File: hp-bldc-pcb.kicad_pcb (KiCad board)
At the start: 4 copper layers, 93 x 53 mm, 109 parts, among them IC101 MCP1790-5002E/DB, IC401 PIC16F1936, IC601 BTN8962TA, IC631 BTN8962TA, IC661 BTN8962TA, T102 SBC817-40LT1G, T103 SBC817-40LT1G

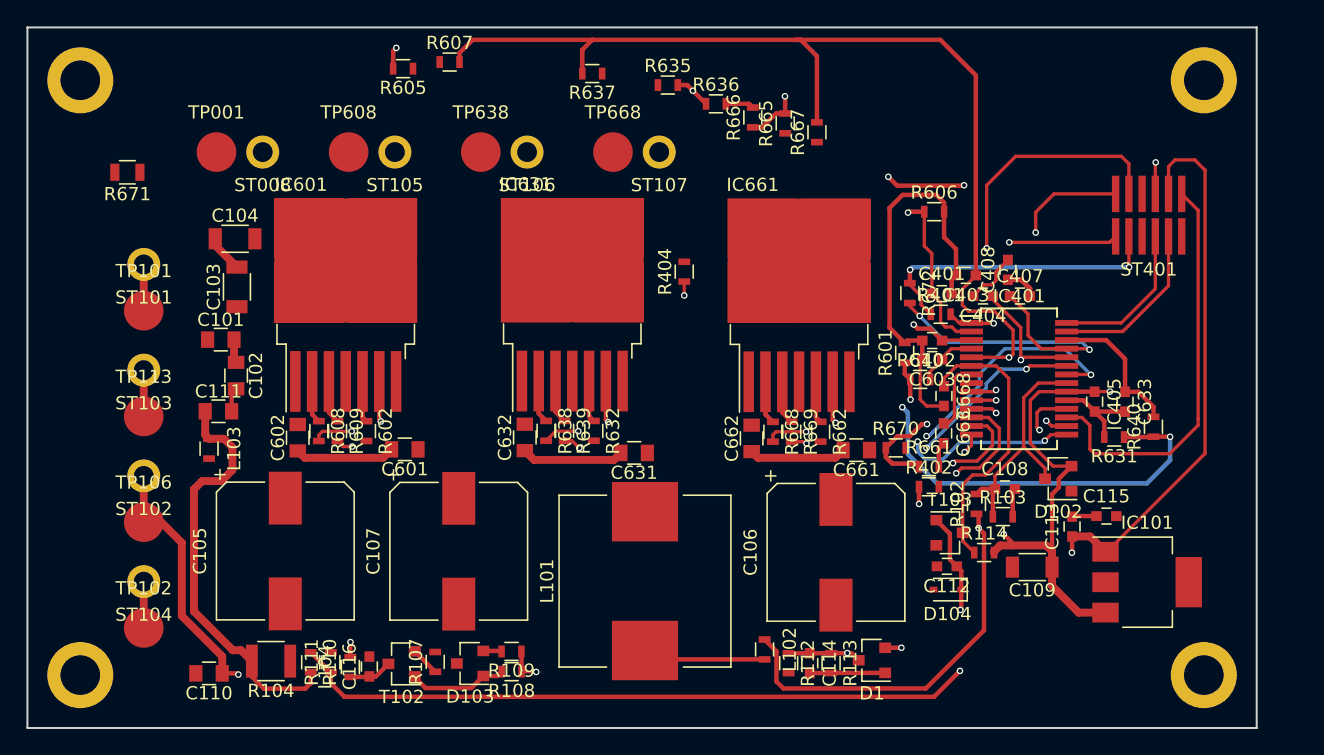
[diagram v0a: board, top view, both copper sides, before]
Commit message: - Finished putting down copper areas.
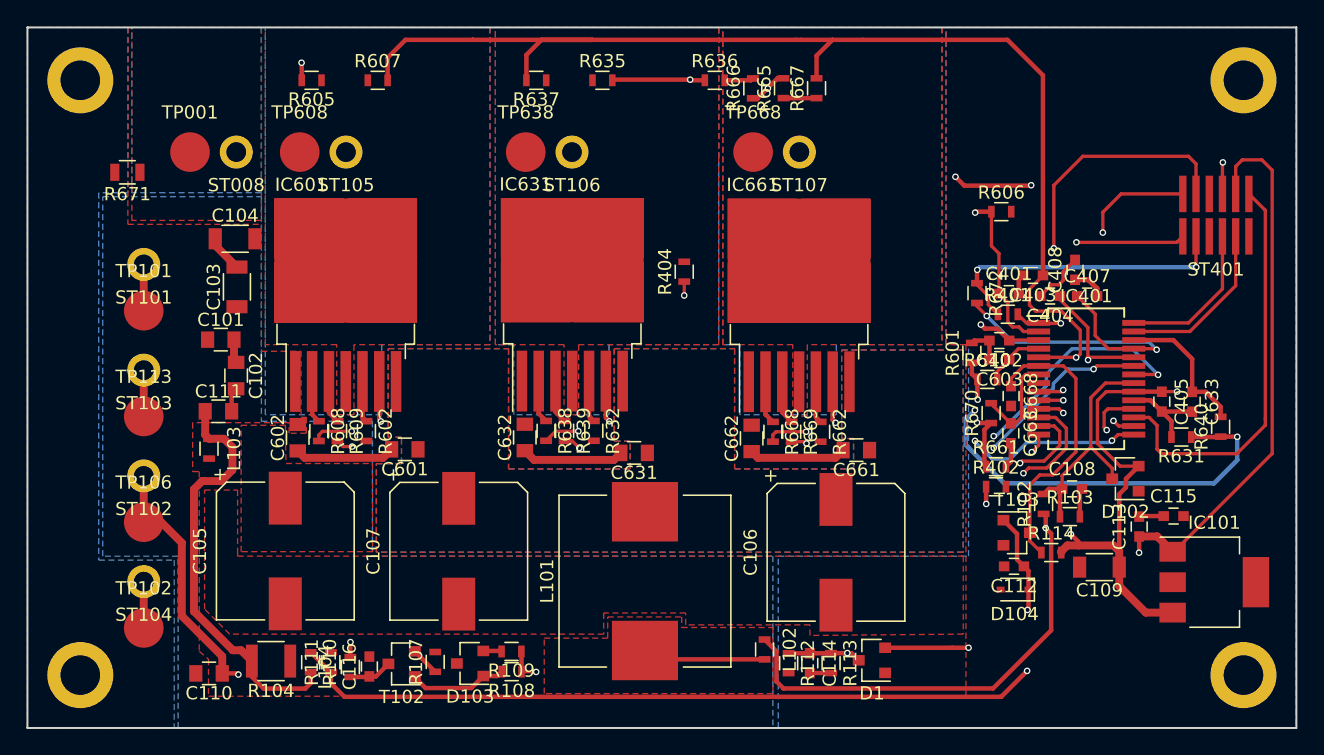
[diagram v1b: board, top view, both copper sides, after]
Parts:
- moved ST107 10.6 mm to (154.4, 78.4)
- moved TP668 10.6 mm to (150.9, 78.4)
- moved R670 7.68 mm to (168.9, 98.2), turned to 90 degrees
- moved R605 6.98 mm to (117.5, 73.0)
- moved R607 5.61 mm to (122.5, 73.0)
- moved C108 5.08 mm to (175.0, 103.9)
- moved C113 5.08 mm to (180.1, 106.8)
- moved C115 5.08 mm to (182.7, 106.0)
- moved C401 5.08 mm to (170.2, 89.1)
- moved C402 5.08 mm to (169.5, 92.7)
- moved C403 5.08 mm to (172.1, 87.8)
- moved C404 5.08 mm to (173.4, 89.3)
- moved C603 5.08 mm to (169.5, 94.1)
- moved C633 5.08 mm to (184.1, 97.3)
- moved C663 5.08 mm to (170.4, 99.7)
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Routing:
- net Earth: track 60.6 -> 30.4 mm
- net PH_1_V_SENSE: track 64.6 -> 77.2 mm
- net PH_SUM_SENSE: track 96.3 -> 108.8 mm
- net PH_2_V_SENSE: track 44.3 -> 54.3 mm
- net Net-(IC631-Pad6): track 56.5 -> 62.0 mm
- net PH_1_EN_FET: track 55.8 -> 61.3 mm
- net PH_1_DIR_FET: track 56.4 -> 61.6 mm
- net DIAG_MON: track 34.6 -> 39.7 mm
- net DIAG_PIC: track 54.2 -> 59.3 mm
- net Net-(C407-Pad1): track 55.0 -> 60.1 mm
- net PH_2_EN_FET: track 32.6 -> 37.7 mm
- net VBATT_2: track 79.8 -> 84.9 mm
- net Net-(IC601-Pad6): track 46.9 -> 52.0 mm
- net PH_3_DIR_FET: track 30.7 -> 35.8 mm
- net PH_2_DIR_FET: track 43.3 -> 48.4 mm
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- added copper zone on B.Cu, net Earth
- added copper zone on F.Cu, net Earth
- added copper zone on In1.Cu, net Earth
- added copper zone on In2.Cu, net Earth
- added copper zone on B.Cu, net Net-(R671-Pad1)
- added copper zone on F.Cu, net Net-(R671-Pad1)
- added copper zone on B.Cu, net PH_1
- added copper zone on F.Cu, net PH_1
- added copper zone on In1.Cu, net PH_1
- added copper zone on In2.Cu, net PH_1
- added copper zone on B.Cu, net PH_2
- added copper zone on F.Cu, net PH_2
- added copper zone on In1.Cu, net PH_2
- added copper zone on In2.Cu, net PH_2
- added copper zone on B.Cu, net PH_3
- added copper zone on F.Cu, net PH_3
- added copper zone on In1.Cu, net PH_3
- added copper zone on In2.Cu, net PH_3
- added copper zone on B.Cu, net VBATT
- added copper zone on F.Cu, net VBATT
- added copper zone on In2.Cu, net VBATT
- added copper zone on B.Cu, net VBATT_INT
- added copper zone on F.Cu, net VBATT_INT
- added copper zone on In2.Cu, net VBATT_INT
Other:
- board size 93 x 53 mm -> 96 x 53 mm

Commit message: - Almost done with PCB.  Need to fix a few errors.
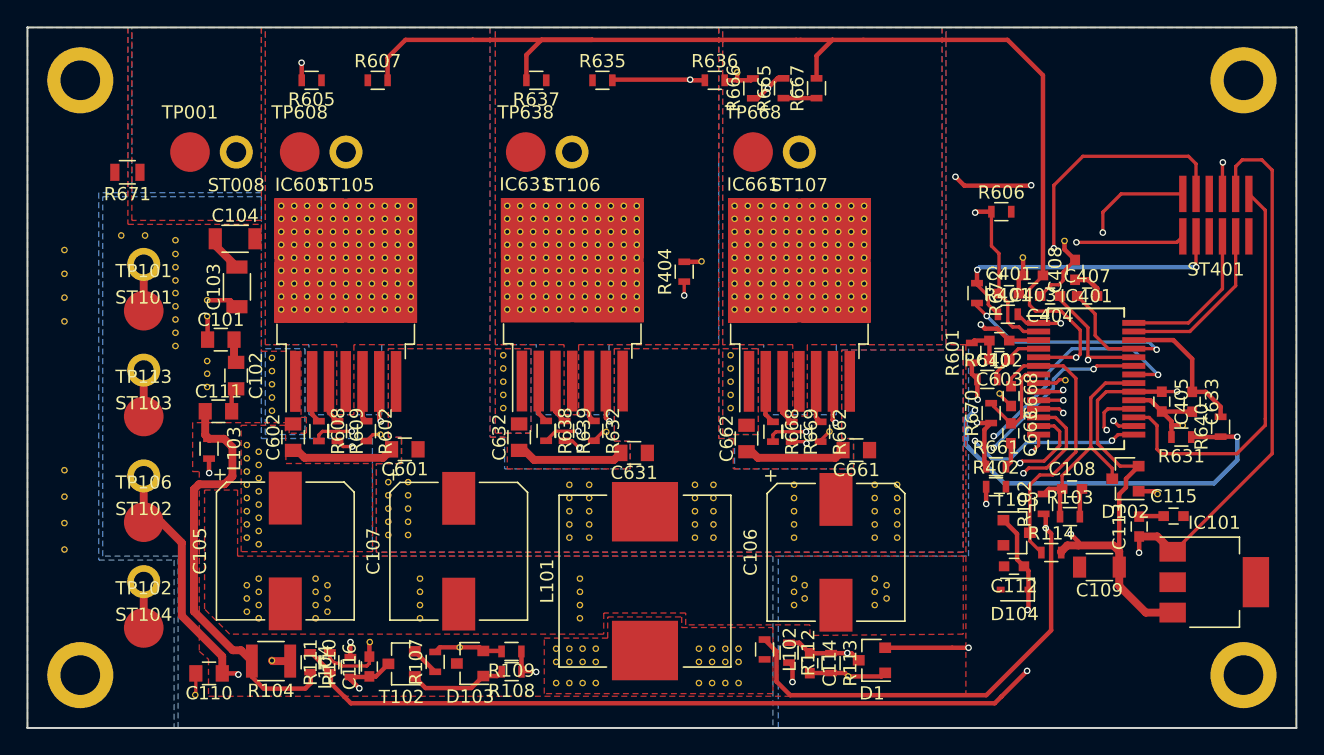
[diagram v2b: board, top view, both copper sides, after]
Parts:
- added REF**: VIA_0.3mm, hp-bldc-pcb:VIA_0.3mm, F.Cu at (174.5, 85.2)
- added REF**: VIA_0.3mm, hp-bldc-pcb:VIA_0.3mm, F.Cu at (161.0, 111.2)
- added REF**: VIA_0.3mm, hp-bldc-pcb:VIA_0.3mm, F.Cu at (147.9, 106.6)
- added REF**: VIA_0.3mm, hp-bldc-pcb:VIA_0.3mm, F.Cu at (147.9, 105.6)
- added REF**: VIA_0.3mm, hp-bldc-pcb:VIA_0.3mm, F.Cu at (147.9, 104.6)
- added REF**: VIA_0.3mm, hp-bldc-pcb:VIA_0.3mm, F.Cu at (147.9, 103.6)
- added REF**: VIA_0.3mm, hp-bldc-pcb:VIA_0.3mm, F.Cu at (146.5, 107.6)
- added REF**: VIA_0.3mm, hp-bldc-pcb:VIA_0.3mm, F.Cu at (146.5, 106.6)
- added REF**: VIA_0.3mm, hp-bldc-pcb:VIA_0.3mm, F.Cu at (146.5, 105.6)
- added REF**: VIA_0.3mm, hp-bldc-pcb:VIA_0.3mm, F.Cu at (146.5, 104.6)
- added REF**: VIA_0.3mm, hp-bldc-pcb:VIA_0.3mm, F.Cu at (146.5, 103.6)
- added REF**: VIA_0.3mm, hp-bldc-pcb:VIA_0.3mm, F.Cu at (138.5, 107.6)
- added REF**: VIA_0.3mm, hp-bldc-pcb:VIA_0.3mm, F.Cu at (160.1, 112.7)
- added REF**: VIA_0.3mm, hp-bldc-pcb:VIA_0.3mm, F.Cu at (138.5, 106.6)
- added REF**: VIA_0.3mm, hp-bldc-pcb:VIA_0.3mm, F.Cu at (138.5, 105.6)
- added REF**: VIA_0.3mm, hp-bldc-pcb:VIA_0.3mm, F.Cu at (138.5, 104.6)
- added REF**: VIA_0.3mm, hp-bldc-pcb:VIA_0.3mm, F.Cu at (138.5, 103.6)
- added REF**: VIA_0.3mm, hp-bldc-pcb:VIA_0.3mm, F.Cu at (137.0, 107.6)
- added REF**: VIA_0.3mm, hp-bldc-pcb:VIA_0.3mm, F.Cu at (137.0, 106.6)
- added REF**: VIA_0.3mm, hp-bldc-pcb:VIA_0.3mm, F.Cu at (137.0, 105.6)
- added REF**: VIA_0.3mm, hp-bldc-pcb:VIA_0.3mm, F.Cu at (137.0, 104.6)
- added REF**: VIA_0.3mm, hp-bldc-pcb:VIA_0.3mm, F.Cu at (137.0, 103.6)
- added REF**: VIA_0.3mm, hp-bldc-pcb:VIA_0.3mm, F.Cu at (124.8, 107.4)
- added REF**: VIA_0.3mm, hp-bldc-pcb:VIA_0.3mm, F.Cu at (160.1, 111.7)
- added REF**: VIA_0.3mm, hp-bldc-pcb:VIA_0.3mm, F.Cu at (124.8, 106.4)
- added REF**: VIA_0.3mm, hp-bldc-pcb:VIA_0.3mm, F.Cu at (124.8, 105.4)
- added REF**: VIA_0.3mm, hp-bldc-pcb:VIA_0.3mm, F.Cu at (124.8, 104.4)
- added REF**: VIA_0.3mm, hp-bldc-pcb:VIA_0.3mm, F.Cu at (124.8, 103.4)
- added REF**: VIA_0.3mm, hp-bldc-pcb:VIA_0.3mm, F.Cu at (123.3, 107.4)
- added REF**: VIA_0.3mm, hp-bldc-pcb:VIA_0.3mm, F.Cu at (123.3, 106.4)
- added REF**: VIA_0.3mm, hp-bldc-pcb:VIA_0.3mm, F.Cu at (123.3, 105.4)
- added REF**: VIA_0.3mm, hp-bldc-pcb:VIA_0.3mm, F.Cu at (123.3, 104.4)
- added REF**: VIA_0.3mm, hp-bldc-pcb:VIA_0.3mm, F.Cu at (123.3, 103.4)
- added REF**: VIA_0.3mm, hp-bldc-pcb:VIA_0.3mm, F.Cu at (112.6, 107.6)
- added REF**: VIA_0.3mm, hp-bldc-pcb:VIA_0.3mm, F.Cu at (160.1, 110.7)
- added REF**: VIA_0.3mm, hp-bldc-pcb:VIA_0.3mm, F.Cu at (112.6, 106.6)
- added REF**: VIA_0.3mm, hp-bldc-pcb:VIA_0.3mm, F.Cu at (112.6, 105.6)
- added REF**: VIA_0.3mm, hp-bldc-pcb:VIA_0.3mm, F.Cu at (112.6, 104.6)
- added REF**: VIA_0.3mm, hp-bldc-pcb:VIA_0.3mm, F.Cu at (112.6, 103.6)
- added REF**: VIA_0.3mm, hp-bldc-pcb:VIA_0.3mm, F.Cu at (112.6, 102.6)
- added REF**: VIA_0.3mm, hp-bldc-pcb:VIA_0.3mm, F.Cu at (112.6, 101.6)
- added REF**: VIA_0.3mm, hp-bldc-pcb:VIA_0.3mm, F.Cu at (112.6, 100.6)
- added REF**: VIA_0.3mm, hp-bldc-pcb:VIA_0.3mm, F.Cu at (113.5, 108.1)
- added REF**: VIA_0.3mm, hp-bldc-pcb:VIA_0.3mm, F.Cu at (113.5, 107.1)
- added REF**: VIA_0.3mm, hp-bldc-pcb:VIA_0.3mm, F.Cu at (113.5, 106.1)
- added REF**: VIA_0.3mm, hp-bldc-pcb:VIA_0.3mm, F.Cu at (154.8, 112.2)
- added REF**: VIA_0.3mm, hp-bldc-pcb:VIA_0.3mm, F.Cu at (113.5, 105.1)
- added REF**: VIA_0.3mm, hp-bldc-pcb:VIA_0.3mm, F.Cu at (113.5, 104.1)
- added REF**: VIA_0.3mm, hp-bldc-pcb:VIA_0.3mm, F.Cu at (113.5, 103.1)
- added REF**: VIA_0.3mm, hp-bldc-pcb:VIA_0.3mm, F.Cu at (113.5, 102.1)
- added REF**: VIA_0.3mm, hp-bldc-pcb:VIA_0.3mm, F.Cu at (113.5, 101.1)
- added REF**: VIA_0.3mm, hp-bldc-pcb:VIA_0.3mm, F.Cu at (107.2, 92.1)
- added REF**: VIA_0.3mm, hp-bldc-pcb:VIA_0.3mm, F.Cu at (107.2, 91.1)
- added REF**: VIA_0.3mm, hp-bldc-pcb:VIA_0.3mm, F.Cu at (107.2, 90.1)
- added REF**: VIA_0.3mm, hp-bldc-pcb:VIA_0.3mm, F.Cu at (107.2, 89.1)
- added REF**: VIA_0.3mm, hp-bldc-pcb:VIA_0.3mm, F.Cu at (107.2, 85.1)
- added REF**: VIA_0.3mm, hp-bldc-pcb:VIA_0.3mm, F.Cu at (154.8, 111.2)
- added REF**: VIA_0.3mm, hp-bldc-pcb:VIA_0.3mm, F.Cu at (103.1, 84.7)
- added REF**: VIA_0.3mm, hp-bldc-pcb:VIA_0.3mm, F.Cu at (109.6, 96.2)
- added REF**: VIA_0.3mm, hp-bldc-pcb:VIA_0.3mm, F.Cu at (109.6, 95.2)
- added REF**: VIA_0.3mm, hp-bldc-pcb:VIA_0.3mm, F.Cu at (109.6, 94.2)
- added REF**: VIA_0.3mm, hp-bldc-pcb:VIA_0.3mm, F.Cu at (109.6, 90.8)
- added REF**: VIA_0.3mm, hp-bldc-pcb:VIA_0.3mm, F.Cu at (109.6, 89.6)
- added REF**: VIA_0.3mm, hp-bldc-pcb:VIA_0.3mm, F.Cu at (114.5, 98.0)
- added REF**: VIA_0.3mm, hp-bldc-pcb:VIA_0.3mm, F.Cu at (114.5, 97.0)
- added REF**: VIA_0.3mm, hp-bldc-pcb:VIA_0.3mm, F.Cu at (114.5, 96.0)
- added REF**: VIA_0.3mm, hp-bldc-pcb:VIA_0.3mm, F.Cu at (114.5, 95.0)
- added REF**: VIA_0.3mm, hp-bldc-pcb:VIA_0.3mm, F.Cu at (154.0, 112.7)
- added REF**: VIA_0.3mm, hp-bldc-pcb:VIA_0.3mm, F.Cu at (114.5, 94.0)
- added REF**: VIA_0.3mm, hp-bldc-pcb:VIA_0.3mm, F.Cu at (132.0, 97.8)
- added REF**: VIA_0.3mm, hp-bldc-pcb:VIA_0.3mm, F.Cu at (132.0, 96.8)
- added REF**: VIA_0.3mm, hp-bldc-pcb:VIA_0.3mm, F.Cu at (132.0, 95.8)
- added REF**: VIA_0.3mm, hp-bldc-pcb:VIA_0.3mm, F.Cu at (132.0, 94.8)
- added REF**: VIA_0.3mm, hp-bldc-pcb:VIA_0.3mm, F.Cu at (132.0, 93.8)
- added REF**: VIA_0.3mm, hp-bldc-pcb:VIA_0.3mm, F.Cu at (149.2, 97.8)
- added REF**: VIA_0.3mm, hp-bldc-pcb:VIA_0.3mm, F.Cu at (149.2, 96.8)
- added REF**: VIA_0.3mm, hp-bldc-pcb:VIA_0.3mm, F.Cu at (149.2, 95.8)
- added REF**: VIA_0.3mm, hp-bldc-pcb:VIA_0.3mm, F.Cu at (149.2, 94.8)
- added REF**: VIA_0.3mm, hp-bldc-pcb:VIA_0.3mm, F.Cu at (154.0, 111.7)
- added REF**: VIA_0.3mm, hp-bldc-pcb:VIA_0.3mm, F.Cu at (149.2, 93.8)
- added REF**: VIA_0.3mm, hp-bldc-pcb:VIA_0.3mm, F.Cu at (147.0, 86.7)
- added REF**: VIA_0.3mm, hp-bldc-pcb:VIA_0.3mm, F.Cu at (149.7, 72.4)
- added REF**: VIA_0.3mm, hp-bldc-pcb:VIA_0.3mm, F.Cu at (125.0, 90.3)
- added REF**: VIA_0.3mm, hp-bldc-pcb:VIA_0.3mm, F.Cu at (125.0, 89.4)
- added REF**: VIA_0.3mm, hp-bldc-pcb:VIA_0.3mm, F.Cu at (125.0, 88.4)
- added REF**: VIA_0.3mm, hp-bldc-pcb:VIA_0.3mm, F.Cu at (125.0, 87.4)
- added REF**: VIA_0.3mm, hp-bldc-pcb:VIA_0.3mm, F.Cu at (125.0, 86.4)
- added REF**: VIA_0.3mm, hp-bldc-pcb:VIA_0.3mm, F.Cu at (125.0, 85.4)
- added REF**: VIA_0.3mm, hp-bldc-pcb:VIA_0.3mm, F.Cu at (125.0, 84.5)
- added REF**: VIA_0.3mm, hp-bldc-pcb:VIA_0.3mm, F.Cu at (154.0, 110.7)
- added REF**: VIA_0.3mm, hp-bldc-pcb:VIA_0.3mm, F.Cu at (125.0, 83.5)
- added REF**: VIA_0.3mm, hp-bldc-pcb:VIA_0.3mm, F.Cu at (125.0, 82.5)
- added REF**: VIA_0.3mm, hp-bldc-pcb:VIA_0.3mm, F.Cu at (124.0, 90.3)
- added REF**: VIA_0.3mm, hp-bldc-pcb:VIA_0.3mm, F.Cu at (124.0, 89.4)
- added REF**: VIA_0.3mm, hp-bldc-pcb:VIA_0.3mm, F.Cu at (124.0, 88.4)
- added REF**: VIA_0.3mm, hp-bldc-pcb:VIA_0.3mm, F.Cu at (124.0, 87.4)
- added REF**: VIA_0.3mm, hp-bldc-pcb:VIA_0.3mm, F.Cu at (124.0, 86.4)
- added REF**: VIA_0.3mm, hp-bldc-pcb:VIA_0.3mm, F.Cu at (124.0, 85.4)
- added REF**: VIA_0.3mm, hp-bldc-pcb:VIA_0.3mm, F.Cu at (124.0, 84.5)
- added REF**: VIA_0.3mm, hp-bldc-pcb:VIA_0.3mm, F.Cu at (124.0, 83.5)
- added REF**: VIA_0.3mm, hp-bldc-pcb:VIA_0.3mm, F.Cu at (137.8, 113.7)
- added REF**: VIA_0.3mm, hp-bldc-pcb:VIA_0.3mm, F.Cu at (124.0, 82.5)
- added REF**: VIA_0.3mm, hp-bldc-pcb:VIA_0.3mm, F.Cu at (123.0, 90.3)
- added REF**: VIA_0.3mm, hp-bldc-pcb:VIA_0.3mm, F.Cu at (123.0, 89.4)
- added REF**: VIA_0.3mm, hp-bldc-pcb:VIA_0.3mm, F.Cu at (123.0, 88.4)
- added REF**: VIA_0.3mm, hp-bldc-pcb:VIA_0.3mm, F.Cu at (123.0, 87.4)
- added REF**: VIA_0.3mm, hp-bldc-pcb:VIA_0.3mm, F.Cu at (123.0, 86.4)
- added REF**: VIA_0.3mm, hp-bldc-pcb:VIA_0.3mm, F.Cu at (123.0, 85.4)
- added REF**: VIA_0.3mm, hp-bldc-pcb:VIA_0.3mm, F.Cu at (123.0, 84.5)
- added REF**: VIA_0.3mm, hp-bldc-pcb:VIA_0.3mm, F.Cu at (123.0, 83.5)
- added REF**: VIA_0.3mm, hp-bldc-pcb:VIA_0.3mm, F.Cu at (123.0, 82.5)
- added REF**: VIA_0.3mm, hp-bldc-pcb:VIA_0.3mm, F.Cu at (171.3, 86.4)
- added REF**: VIA_0.3mm, hp-bldc-pcb:VIA_0.3mm, F.Cu at (137.8, 112.7)
- added REF**: VIA_0.3mm, hp-bldc-pcb:VIA_0.3mm, F.Cu at (122.1, 90.3)
- added REF**: VIA_0.3mm, hp-bldc-pcb:VIA_0.3mm, F.Cu at (122.1, 89.4)
- added REF**: VIA_0.3mm, hp-bldc-pcb:VIA_0.3mm, F.Cu at (122.1, 88.4)
- added REF**: VIA_0.3mm, hp-bldc-pcb:VIA_0.3mm, F.Cu at (122.1, 87.4)
- added REF**: VIA_0.3mm, hp-bldc-pcb:VIA_0.3mm, F.Cu at (122.1, 86.4)
- added REF**: VIA_0.3mm, hp-bldc-pcb:VIA_0.3mm, F.Cu at (122.1, 85.4)
- added REF**: VIA_0.3mm, hp-bldc-pcb:VIA_0.3mm, F.Cu at (122.1, 84.5)
- added REF**: VIA_0.3mm, hp-bldc-pcb:VIA_0.3mm, F.Cu at (122.1, 83.5)
- added REF**: VIA_0.3mm, hp-bldc-pcb:VIA_0.3mm, F.Cu at (122.1, 82.5)
- added REF**: VIA_0.3mm, hp-bldc-pcb:VIA_0.3mm, F.Cu at (121.1, 90.3)
- added REF**: VIA_0.3mm, hp-bldc-pcb:VIA_0.3mm, F.Cu at (137.8, 111.7)
- added REF**: VIA_0.3mm, hp-bldc-pcb:VIA_0.3mm, F.Cu at (121.1, 89.4)
- added REF**: VIA_0.3mm, hp-bldc-pcb:VIA_0.3mm, F.Cu at (121.1, 88.4)
- added REF**: VIA_0.3mm, hp-bldc-pcb:VIA_0.3mm, F.Cu at (121.1, 87.4)
- added REF**: VIA_0.3mm, hp-bldc-pcb:VIA_0.3mm, F.Cu at (121.1, 86.4)
- added REF**: VIA_0.3mm, hp-bldc-pcb:VIA_0.3mm, F.Cu at (121.1, 85.4)
- added REF**: VIA_0.3mm, hp-bldc-pcb:VIA_0.3mm, F.Cu at (121.1, 84.5)
- added REF**: VIA_0.3mm, hp-bldc-pcb:VIA_0.3mm, F.Cu at (121.1, 83.5)
- added REF**: VIA_0.3mm, hp-bldc-pcb:VIA_0.3mm, F.Cu at (121.1, 82.5)
- added REF**: VIA_0.3mm, hp-bldc-pcb:VIA_0.3mm, F.Cu at (120.1, 90.3)
- added REF**: VIA_0.3mm, hp-bldc-pcb:VIA_0.3mm, F.Cu at (120.1, 89.4)
- added REF**: VIA_0.3mm, hp-bldc-pcb:VIA_0.3mm, F.Cu at (137.8, 110.7)
- added REF**: VIA_0.3mm, hp-bldc-pcb:VIA_0.3mm, F.Cu at (120.1, 88.4)
- added REF**: VIA_0.3mm, hp-bldc-pcb:VIA_0.3mm, F.Cu at (120.1, 87.4)
- added REF**: VIA_0.3mm, hp-bldc-pcb:VIA_0.3mm, F.Cu at (120.1, 86.4)
- added REF**: VIA_0.3mm, hp-bldc-pcb:VIA_0.3mm, F.Cu at (120.1, 85.4)
- added REF**: VIA_0.3mm, hp-bldc-pcb:VIA_0.3mm, F.Cu at (120.1, 84.5)
- added REF**: VIA_0.3mm, hp-bldc-pcb:VIA_0.3mm, F.Cu at (120.1, 83.5)
- added REF**: VIA_0.3mm, hp-bldc-pcb:VIA_0.3mm, F.Cu at (120.1, 82.5)
- added REF**: VIA_0.3mm, hp-bldc-pcb:VIA_0.3mm, F.Cu at (119.1, 90.3)
- added REF**: VIA_0.3mm, hp-bldc-pcb:VIA_0.3mm, F.Cu at (119.1, 89.4)
- added REF**: VIA_0.3mm, hp-bldc-pcb:VIA_0.3mm, F.Cu at (119.1, 88.4)
- added REF**: VIA_0.3mm, hp-bldc-pcb:VIA_0.3mm, F.Cu at (125.7, 113.7)
- added REF**: VIA_0.3mm, hp-bldc-pcb:VIA_0.3mm, F.Cu at (119.1, 87.4)
- added REF**: VIA_0.3mm, hp-bldc-pcb:VIA_0.3mm, F.Cu at (119.1, 86.4)
- added REF**: VIA_0.3mm, hp-bldc-pcb:VIA_0.3mm, F.Cu at (119.1, 85.4)
- added REF**: VIA_0.3mm, hp-bldc-pcb:VIA_0.3mm, F.Cu at (119.1, 84.5)
- added REF**: VIA_0.3mm, hp-bldc-pcb:VIA_0.3mm, F.Cu at (119.1, 83.5)
- added REF**: VIA_0.3mm, hp-bldc-pcb:VIA_0.3mm, F.Cu at (119.1, 82.5)
- added REF**: VIA_0.3mm, hp-bldc-pcb:VIA_0.3mm, F.Cu at (118.1, 90.3)
- added REF**: VIA_0.3mm, hp-bldc-pcb:VIA_0.3mm, F.Cu at (118.1, 89.4)
- added REF**: VIA_0.3mm, hp-bldc-pcb:VIA_0.3mm, F.Cu at (118.1, 88.4)
- added REF**: VIA_0.3mm, hp-bldc-pcb:VIA_0.3mm, F.Cu at (118.1, 87.4)
- added REF**: VIA_0.3mm, hp-bldc-pcb:VIA_0.3mm, F.Cu at (125.7, 112.7)
- added REF**: VIA_0.3mm, hp-bldc-pcb:VIA_0.3mm, F.Cu at (118.1, 86.4)
- added REF**: VIA_0.3mm, hp-bldc-pcb:VIA_0.3mm, F.Cu at (118.1, 85.4)
- added REF**: VIA_0.3mm, hp-bldc-pcb:VIA_0.3mm, F.Cu at (118.1, 84.5)
- added REF**: VIA_0.3mm, hp-bldc-pcb:VIA_0.3mm, F.Cu at (118.1, 83.5)
- added REF**: VIA_0.3mm, hp-bldc-pcb:VIA_0.3mm, F.Cu at (118.1, 82.5)
- added REF**: VIA_0.3mm, hp-bldc-pcb:VIA_0.3mm, F.Cu at (117.2, 90.3)
- added REF**: VIA_0.3mm, hp-bldc-pcb:VIA_0.3mm, F.Cu at (117.2, 89.4)
- added REF**: VIA_0.3mm, hp-bldc-pcb:VIA_0.3mm, F.Cu at (117.2, 88.4)
- added REF**: VIA_0.3mm, hp-bldc-pcb:VIA_0.3mm, F.Cu at (117.2, 87.4)
- added REF**: VIA_0.3mm, hp-bldc-pcb:VIA_0.3mm, F.Cu at (117.2, 86.4)
- added REF**: VIA_0.3mm, hp-bldc-pcb:VIA_0.3mm, F.Cu at (125.7, 111.7)
- added REF**: VIA_0.3mm, hp-bldc-pcb:VIA_0.3mm, F.Cu at (117.2, 85.4)
- added REF**: VIA_0.3mm, hp-bldc-pcb:VIA_0.3mm, F.Cu at (117.2, 84.5)
- added REF**: VIA_0.3mm, hp-bldc-pcb:VIA_0.3mm, F.Cu at (117.2, 83.5)
- added REF**: VIA_0.3mm, hp-bldc-pcb:VIA_0.3mm, F.Cu at (117.2, 82.5)
- added REF**: VIA_0.3mm, hp-bldc-pcb:VIA_0.3mm, F.Cu at (116.2, 90.3)
- added REF**: VIA_0.3mm, hp-bldc-pcb:VIA_0.3mm, F.Cu at (116.2, 89.4)
- added REF**: VIA_0.3mm, hp-bldc-pcb:VIA_0.3mm, F.Cu at (116.2, 88.4)
- added REF**: VIA_0.3mm, hp-bldc-pcb:VIA_0.3mm, F.Cu at (116.2, 87.4)
- added REF**: VIA_0.3mm, hp-bldc-pcb:VIA_0.3mm, F.Cu at (116.2, 86.4)
- added REF**: VIA_0.3mm, hp-bldc-pcb:VIA_0.3mm, F.Cu at (116.2, 85.4)
- added REF**: VIA_0.3mm, hp-bldc-pcb:VIA_0.3mm, F.Cu at (125.7, 110.7)
- added REF**: VIA_0.3mm, hp-bldc-pcb:VIA_0.3mm, F.Cu at (116.2, 84.5)
- added REF**: VIA_0.3mm, hp-bldc-pcb:VIA_0.3mm, F.Cu at (116.2, 83.5)
- added REF**: VIA_0.3mm, hp-bldc-pcb:VIA_0.3mm, F.Cu at (116.2, 82.5)
- added REF**: VIA_0.3mm, hp-bldc-pcb:VIA_0.3mm, F.Cu at (115.2, 90.3)
- added REF**: VIA_0.3mm, hp-bldc-pcb:VIA_0.3mm, F.Cu at (115.2, 89.4)
- added REF**: VIA_0.3mm, hp-bldc-pcb:VIA_0.3mm, F.Cu at (115.2, 88.4)
- added REF**: VIA_0.3mm, hp-bldc-pcb:VIA_0.3mm, F.Cu at (115.2, 87.4)
- added REF**: VIA_0.3mm, hp-bldc-pcb:VIA_0.3mm, F.Cu at (115.2, 86.4)
- added REF**: VIA_0.3mm, hp-bldc-pcb:VIA_0.3mm, F.Cu at (115.2, 85.4)
- added REF**: VIA_0.3mm, hp-bldc-pcb:VIA_0.3mm, F.Cu at (115.2, 84.5)
- added REF**: VIA_0.3mm, hp-bldc-pcb:VIA_0.3mm, F.Cu at (118.7, 113.2)
- added REF**: VIA_0.3mm, hp-bldc-pcb:VIA_0.3mm, F.Cu at (115.2, 83.5)
- added REF**: VIA_0.3mm, hp-bldc-pcb:VIA_0.3mm, F.Cu at (115.2, 82.5)
- added REF**: VIA_0.3mm, hp-bldc-pcb:VIA_0.3mm, F.Cu at (149.5, 82.5)
- added REF**: VIA_0.3mm, hp-bldc-pcb:VIA_0.3mm, F.Cu at (142.1, 90.3)
- added REF**: VIA_0.3mm, hp-bldc-pcb:VIA_0.3mm, F.Cu at (142.1, 89.4)
- added REF**: VIA_0.3mm, hp-bldc-pcb:VIA_0.3mm, F.Cu at (142.1, 88.4)
- added REF**: VIA_0.3mm, hp-bldc-pcb:VIA_0.3mm, F.Cu at (142.1, 87.4)
- added REF**: VIA_0.3mm, hp-bldc-pcb:VIA_0.3mm, F.Cu at (142.1, 86.4)
- added REF**: VIA_0.3mm, hp-bldc-pcb:VIA_0.3mm, F.Cu at (142.1, 85.4)
- added REF**: VIA_0.3mm, hp-bldc-pcb:VIA_0.3mm, F.Cu at (142.1, 84.5)
- added REF**: VIA_0.3mm, hp-bldc-pcb:VIA_0.3mm, F.Cu at (118.7, 112.2)
- added REF**: VIA_0.3mm, hp-bldc-pcb:VIA_0.3mm, F.Cu at (142.1, 83.5)
- added REF**: VIA_0.3mm, hp-bldc-pcb:VIA_0.3mm, F.Cu at (142.1, 82.5)
- added REF**: VIA_0.3mm, hp-bldc-pcb:VIA_0.3mm, F.Cu at (141.1, 90.3)
- added REF**: VIA_0.3mm, hp-bldc-pcb:VIA_0.3mm, F.Cu at (141.1, 89.4)
- added REF**: VIA_0.3mm, hp-bldc-pcb:VIA_0.3mm, F.Cu at (141.1, 88.4)
- added REF**: VIA_0.3mm, hp-bldc-pcb:VIA_0.3mm, F.Cu at (141.1, 87.4)
- added REF**: VIA_0.3mm, hp-bldc-pcb:VIA_0.3mm, F.Cu at (141.1, 86.4)
- added REF**: VIA_0.3mm, hp-bldc-pcb:VIA_0.3mm, F.Cu at (141.1, 85.4)
- added REF**: VIA_0.3mm, hp-bldc-pcb:VIA_0.3mm, F.Cu at (141.1, 84.5)
- added REF**: VIA_0.3mm, hp-bldc-pcb:VIA_0.3mm, F.Cu at (141.1, 83.5)
- added REF**: VIA_0.3mm, hp-bldc-pcb:VIA_0.3mm, F.Cu at (118.7, 111.2)
- added REF**: VIA_0.3mm, hp-bldc-pcb:VIA_0.3mm, F.Cu at (141.1, 82.5)
- added REF**: VIA_0.3mm, hp-bldc-pcb:VIA_0.3mm, F.Cu at (140.1, 90.3)
- added REF**: VIA_0.3mm, hp-bldc-pcb:VIA_0.3mm, F.Cu at (140.1, 89.4)
- added REF**: VIA_0.3mm, hp-bldc-pcb:VIA_0.3mm, F.Cu at (140.1, 88.4)
- added REF**: VIA_0.3mm, hp-bldc-pcb:VIA_0.3mm, F.Cu at (140.1, 87.4)
- added REF**: VIA_0.3mm, hp-bldc-pcb:VIA_0.3mm, F.Cu at (140.1, 86.4)
- added REF**: VIA_0.3mm, hp-bldc-pcb:VIA_0.3mm, F.Cu at (140.1, 85.4)
- added REF**: VIA_0.3mm, hp-bldc-pcb:VIA_0.3mm, F.Cu at (140.1, 84.5)
- added REF**: VIA_0.3mm, hp-bldc-pcb:VIA_0.3mm, F.Cu at (140.1, 83.5)
- added REF**: VIA_0.3mm, hp-bldc-pcb:VIA_0.3mm, F.Cu at (140.1, 82.5)
- added REF**: VIA_0.3mm, hp-bldc-pcb:VIA_0.3mm, F.Cu at (169.6, 96.7)
- added REF**: VIA_0.3mm, hp-bldc-pcb:VIA_0.3mm, F.Cu at (117.8, 113.7)
- added REF**: VIA_0.3mm, hp-bldc-pcb:VIA_0.3mm, F.Cu at (139.2, 90.3)
- added REF**: VIA_0.3mm, hp-bldc-pcb:VIA_0.3mm, F.Cu at (139.2, 89.4)
- added REF**: VIA_0.3mm, hp-bldc-pcb:VIA_0.3mm, F.Cu at (139.2, 88.4)
- added REF**: VIA_0.3mm, hp-bldc-pcb:VIA_0.3mm, F.Cu at (139.2, 87.4)
- added REF**: VIA_0.3mm, hp-bldc-pcb:VIA_0.3mm, F.Cu at (139.2, 86.4)
- added REF**: VIA_0.3mm, hp-bldc-pcb:VIA_0.3mm, F.Cu at (139.2, 85.4)
- added REF**: VIA_0.3mm, hp-bldc-pcb:VIA_0.3mm, F.Cu at (139.2, 84.5)
- added REF**: VIA_0.3mm, hp-bldc-pcb:VIA_0.3mm, F.Cu at (139.2, 83.5)
- added REF**: VIA_0.3mm, hp-bldc-pcb:VIA_0.3mm, F.Cu at (139.2, 82.5)
- added REF**: VIA_0.3mm, hp-bldc-pcb:VIA_0.3mm, F.Cu at (138.2, 90.3)
- added REF**: VIA_0.3mm, hp-bldc-pcb:VIA_0.3mm, F.Cu at (117.8, 112.7)
- added REF**: VIA_0.3mm, hp-bldc-pcb:VIA_0.3mm, F.Cu at (138.2, 89.4)
- added REF**: VIA_0.3mm, hp-bldc-pcb:VIA_0.3mm, F.Cu at (138.2, 88.4)
- added REF**: VIA_0.3mm, hp-bldc-pcb:VIA_0.3mm, F.Cu at (138.2, 87.4)
- added REF**: VIA_0.3mm, hp-bldc-pcb:VIA_0.3mm, F.Cu at (138.2, 86.4)
- added REF**: VIA_0.3mm, hp-bldc-pcb:VIA_0.3mm, F.Cu at (138.2, 85.4)
- added REF**: VIA_0.3mm, hp-bldc-pcb:VIA_0.3mm, F.Cu at (138.2, 84.5)
- added REF**: VIA_0.3mm, hp-bldc-pcb:VIA_0.3mm, F.Cu at (138.2, 83.5)
- added REF**: VIA_0.3mm, hp-bldc-pcb:VIA_0.3mm, F.Cu at (138.2, 82.5)
- added REF**: VIA_0.3mm, hp-bldc-pcb:VIA_0.3mm, F.Cu at (137.2, 90.3)
- added REF**: VIA_0.3mm, hp-bldc-pcb:VIA_0.3mm, F.Cu at (137.2, 89.4)
- added REF**: VIA_0.3mm, hp-bldc-pcb:VIA_0.3mm, F.Cu at (117.8, 111.7)
- added REF**: VIA_0.3mm, hp-bldc-pcb:VIA_0.3mm, F.Cu at (137.2, 88.4)
- added REF**: VIA_0.3mm, hp-bldc-pcb:VIA_0.3mm, F.Cu at (137.2, 87.4)
- added REF**: VIA_0.3mm, hp-bldc-pcb:VIA_0.3mm, F.Cu at (137.2, 86.4)
- added REF**: VIA_0.3mm, hp-bldc-pcb:VIA_0.3mm, F.Cu at (137.2, 85.4)
- added REF**: VIA_0.3mm, hp-bldc-pcb:VIA_0.3mm, F.Cu at (137.2, 84.5)
- added REF**: VIA_0.3mm, hp-bldc-pcb:VIA_0.3mm, F.Cu at (137.2, 83.5)
- added REF**: VIA_0.3mm, hp-bldc-pcb:VIA_0.3mm, F.Cu at (137.2, 82.5)
- added REF**: VIA_0.3mm, hp-bldc-pcb:VIA_0.3mm, F.Cu at (136.2, 90.3)
- added REF**: VIA_0.3mm, hp-bldc-pcb:VIA_0.3mm, F.Cu at (136.2, 89.4)
- added REF**: VIA_0.3mm, hp-bldc-pcb:VIA_0.3mm, F.Cu at (136.2, 88.4)
- added REF**: VIA_0.3mm, hp-bldc-pcb:VIA_0.3mm, F.Cu at (117.8, 110.7)
- added REF**: VIA_0.3mm, hp-bldc-pcb:VIA_0.3mm, F.Cu at (136.2, 87.4)
- added REF**: VIA_0.3mm, hp-bldc-pcb:VIA_0.3mm, F.Cu at (136.2, 86.4)
- added REF**: VIA_0.3mm, hp-bldc-pcb:VIA_0.3mm, F.Cu at (136.2, 85.4)
- added REF**: VIA_0.3mm, hp-bldc-pcb:VIA_0.3mm, F.Cu at (136.2, 84.5)
- added REF**: VIA_0.3mm, hp-bldc-pcb:VIA_0.3mm, F.Cu at (136.2, 83.5)
- added REF**: VIA_0.3mm, hp-bldc-pcb:VIA_0.3mm, F.Cu at (136.2, 82.5)
- added REF**: VIA_0.3mm, hp-bldc-pcb:VIA_0.3mm, F.Cu at (135.2, 90.3)
- added REF**: VIA_0.3mm, hp-bldc-pcb:VIA_0.3mm, F.Cu at (135.2, 89.4)
- added REF**: VIA_0.3mm, hp-bldc-pcb:VIA_0.3mm, F.Cu at (135.2, 88.4)
- added REF**: VIA_0.3mm, hp-bldc-pcb:VIA_0.3mm, F.Cu at (135.2, 87.4)
- added REF**: VIA_0.3mm, hp-bldc-pcb:VIA_0.3mm, F.Cu at (112.6, 113.2)
- added REF**: VIA_0.3mm, hp-bldc-pcb:VIA_0.3mm, F.Cu at (135.2, 86.4)
- added REF**: VIA_0.3mm, hp-bldc-pcb:VIA_0.3mm, F.Cu at (135.2, 85.4)
- added REF**: VIA_0.3mm, hp-bldc-pcb:VIA_0.3mm, F.Cu at (135.2, 84.5)
- added REF**: VIA_0.3mm, hp-bldc-pcb:VIA_0.3mm, F.Cu at (135.2, 83.5)
- added REF**: VIA_0.3mm, hp-bldc-pcb:VIA_0.3mm, F.Cu at (135.2, 82.5)
- added REF**: VIA_0.3mm, hp-bldc-pcb:VIA_0.3mm, F.Cu at (134.3, 90.3)
- added REF**: VIA_0.3mm, hp-bldc-pcb:VIA_0.3mm, F.Cu at (134.3, 89.4)
- added REF**: VIA_0.3mm, hp-bldc-pcb:VIA_0.3mm, F.Cu at (134.3, 88.4)
- added REF**: VIA_0.3mm, hp-bldc-pcb:VIA_0.3mm, F.Cu at (134.3, 87.4)
- added REF**: VIA_0.3mm, hp-bldc-pcb:VIA_0.3mm, F.Cu at (134.3, 86.4)
- added REF**: VIA_0.3mm, hp-bldc-pcb:VIA_0.3mm, F.Cu at (112.6, 112.2)
- added REF**: VIA_0.3mm, hp-bldc-pcb:VIA_0.3mm, F.Cu at (134.3, 85.4)
- added REF**: VIA_0.3mm, hp-bldc-pcb:VIA_0.3mm, F.Cu at (134.3, 84.5)
- added REF**: VIA_0.3mm, hp-bldc-pcb:VIA_0.3mm, F.Cu at (134.3, 83.5)
- added REF**: VIA_0.3mm, hp-bldc-pcb:VIA_0.3mm, F.Cu at (134.3, 82.5)
- added REF**: VIA_0.3mm, hp-bldc-pcb:VIA_0.3mm, F.Cu at (133.3, 90.3)
- added REF**: VIA_0.3mm, hp-bldc-pcb:VIA_0.3mm, F.Cu at (133.3, 89.4)
- added REF**: VIA_0.3mm, hp-bldc-pcb:VIA_0.3mm, F.Cu at (133.3, 88.4)
- added REF**: VIA_0.3mm, hp-bldc-pcb:VIA_0.3mm, F.Cu at (133.3, 87.4)
- added REF**: VIA_0.3mm, hp-bldc-pcb:VIA_0.3mm, F.Cu at (133.3, 86.4)
- added REF**: VIA_0.3mm, hp-bldc-pcb:VIA_0.3mm, F.Cu at (133.3, 85.4)
- added REF**: VIA_0.3mm, hp-bldc-pcb:VIA_0.3mm, F.Cu at (112.6, 111.2)
- added REF**: VIA_0.3mm, hp-bldc-pcb:VIA_0.3mm, F.Cu at (133.3, 84.5)
- added REF**: VIA_0.3mm, hp-bldc-pcb:VIA_0.3mm, F.Cu at (133.3, 83.5)
- added REF**: VIA_0.3mm, hp-bldc-pcb:VIA_0.3mm, F.Cu at (133.3, 82.5)
- added REF**: VIA_0.3mm, hp-bldc-pcb:VIA_0.3mm, F.Cu at (132.3, 90.3)
- added REF**: VIA_0.3mm, hp-bldc-pcb:VIA_0.3mm, F.Cu at (132.3, 89.4)
- added REF**: VIA_0.3mm, hp-bldc-pcb:VIA_0.3mm, F.Cu at (132.3, 88.4)
- added REF**: VIA_0.3mm, hp-bldc-pcb:VIA_0.3mm, F.Cu at (132.3, 87.4)
- added REF**: VIA_0.3mm, hp-bldc-pcb:VIA_0.3mm, F.Cu at (132.3, 86.4)
- added REF**: VIA_0.3mm, hp-bldc-pcb:VIA_0.3mm, F.Cu at (132.3, 85.4)
- added REF**: VIA_0.3mm, hp-bldc-pcb:VIA_0.3mm, F.Cu at (132.3, 84.5)
- added REF**: VIA_0.3mm, hp-bldc-pcb:VIA_0.3mm, F.Cu at (113.5, 113.7)
- added REF**: VIA_0.3mm, hp-bldc-pcb:VIA_0.3mm, F.Cu at (132.3, 83.5)
- added REF**: VIA_0.3mm, hp-bldc-pcb:VIA_0.3mm, F.Cu at (132.3, 82.5)
- added REF**: VIA_0.3mm, hp-bldc-pcb:VIA_0.3mm, F.Cu at (159.3, 90.3)
- added REF**: VIA_0.3mm, hp-bldc-pcb:VIA_0.3mm, F.Cu at (159.3, 89.4)
- added REF**: VIA_0.3mm, hp-bldc-pcb:VIA_0.3mm, F.Cu at (159.3, 88.4)
- added REF**: VIA_0.3mm, hp-bldc-pcb:VIA_0.3mm, F.Cu at (159.3, 87.4)
- added REF**: VIA_0.3mm, hp-bldc-pcb:VIA_0.3mm, F.Cu at (159.3, 86.4)
- added REF**: VIA_0.3mm, hp-bldc-pcb:VIA_0.3mm, F.Cu at (159.3, 85.4)
- added REF**: VIA_0.3mm, hp-bldc-pcb:VIA_0.3mm, F.Cu at (159.3, 84.5)
- added REF**: VIA_0.3mm, hp-bldc-pcb:VIA_0.3mm, F.Cu at (159.3, 83.5)
- added REF**: VIA_0.3mm, hp-bldc-pcb:VIA_0.3mm, F.Cu at (113.5, 112.7)
- added REF**: VIA_0.3mm, hp-bldc-pcb:VIA_0.3mm, F.Cu at (159.3, 82.5)
- added REF**: VIA_0.3mm, hp-bldc-pcb:VIA_0.3mm, F.Cu at (158.3, 90.3)
- added REF**: VIA_0.3mm, hp-bldc-pcb:VIA_0.3mm, F.Cu at (158.3, 89.4)
- added REF**: VIA_0.3mm, hp-bldc-pcb:VIA_0.3mm, F.Cu at (158.3, 88.4)
- added REF**: VIA_0.3mm, hp-bldc-pcb:VIA_0.3mm, F.Cu at (158.3, 87.4)
- added REF**: VIA_0.3mm, hp-bldc-pcb:VIA_0.3mm, F.Cu at (158.3, 86.4)
- added REF**: VIA_0.3mm, hp-bldc-pcb:VIA_0.3mm, F.Cu at (158.3, 85.4)
- added REF**: VIA_0.3mm, hp-bldc-pcb:VIA_0.3mm, F.Cu at (158.3, 84.5)
- added REF**: VIA_0.3mm, hp-bldc-pcb:VIA_0.3mm, F.Cu at (158.3, 83.5)
- added REF**: VIA_0.3mm, hp-bldc-pcb:VIA_0.3mm, F.Cu at (158.3, 82.5)
- added REF**: VIA_0.3mm, hp-bldc-pcb:VIA_0.3mm, F.Cu at (113.5, 111.7)
- added REF**: VIA_0.3mm, hp-bldc-pcb:VIA_0.3mm, F.Cu at (157.3, 90.3)
- added REF**: VIA_0.3mm, hp-bldc-pcb:VIA_0.3mm, F.Cu at (157.3, 89.4)
- added REF**: VIA_0.3mm, hp-bldc-pcb:VIA_0.3mm, F.Cu at (157.3, 88.4)
- added REF**: VIA_0.3mm, hp-bldc-pcb:VIA_0.3mm, F.Cu at (157.3, 87.4)
- added REF**: VIA_0.3mm, hp-bldc-pcb:VIA_0.3mm, F.Cu at (157.3, 86.4)
- added REF**: VIA_0.3mm, hp-bldc-pcb:VIA_0.3mm, F.Cu at (157.3, 85.4)
- added REF**: VIA_0.3mm, hp-bldc-pcb:VIA_0.3mm, F.Cu at (157.3, 84.5)
- added REF**: VIA_0.3mm, hp-bldc-pcb:VIA_0.3mm, F.Cu at (157.3, 83.5)
- added REF**: VIA_0.3mm, hp-bldc-pcb:VIA_0.3mm, F.Cu at (157.3, 82.5)
- added REF**: VIA_0.3mm, hp-bldc-pcb:VIA_0.3mm, F.Cu at (156.4, 90.3)
- added REF**: VIA_0.3mm, hp-bldc-pcb:VIA_0.3mm, F.Cu at (174.5, 95.7)
- added REF**: VIA_0.3mm, hp-bldc-pcb:VIA_0.3mm, F.Cu at (113.5, 110.7)
- added REF**: VIA_0.3mm, hp-bldc-pcb:VIA_0.3mm, F.Cu at (156.4, 89.4)
- added REF**: VIA_0.3mm, hp-bldc-pcb:VIA_0.3mm, F.Cu at (156.4, 88.4)
- added REF**: VIA_0.3mm, hp-bldc-pcb:VIA_0.3mm, F.Cu at (156.4, 87.4)
- added REF**: VIA_0.3mm, hp-bldc-pcb:VIA_0.3mm, F.Cu at (156.4, 86.4)
- added REF**: VIA_0.3mm, hp-bldc-pcb:VIA_0.3mm, F.Cu at (156.4, 85.4)
- added REF**: VIA_0.3mm, hp-bldc-pcb:VIA_0.3mm, F.Cu at (156.4, 84.5)
- added REF**: VIA_0.3mm, hp-bldc-pcb:VIA_0.3mm, F.Cu at (156.4, 83.5)
- added REF**: VIA_0.3mm, hp-bldc-pcb:VIA_0.3mm, F.Cu at (156.4, 82.5)
- added REF**: VIA_0.3mm, hp-bldc-pcb:VIA_0.3mm, F.Cu at (155.4, 90.3)
- added REF**: VIA_0.3mm, hp-bldc-pcb:VIA_0.3mm, F.Cu at (155.4, 89.4)
- added REF**: VIA_0.3mm, hp-bldc-pcb:VIA_0.3mm, F.Cu at (121.9, 115.5)
- added REF**: VIA_0.3mm, hp-bldc-pcb:VIA_0.3mm, F.Cu at (155.4, 88.4)
- added REF**: VIA_0.3mm, hp-bldc-pcb:VIA_0.3mm, F.Cu at (155.4, 87.4)
- added REF**: VIA_0.3mm, hp-bldc-pcb:VIA_0.3mm, F.Cu at (155.4, 86.4)
- added REF**: VIA_0.3mm, hp-bldc-pcb:VIA_0.3mm, F.Cu at (155.4, 85.4)
- added REF**: VIA_0.3mm, hp-bldc-pcb:VIA_0.3mm, F.Cu at (155.4, 84.5)
- added REF**: VIA_0.3mm, hp-bldc-pcb:VIA_0.3mm, F.Cu at (155.4, 83.5)
- added REF**: VIA_0.3mm, hp-bldc-pcb:VIA_0.3mm, F.Cu at (155.4, 82.5)
- added REF**: VIA_0.3mm, hp-bldc-pcb:VIA_0.3mm, F.Cu at (154.4, 90.3)
- added REF**: VIA_0.3mm, hp-bldc-pcb:VIA_0.3mm, F.Cu at (154.4, 89.4)
- added REF**: VIA_0.3mm, hp-bldc-pcb:VIA_0.3mm, F.Cu at (154.4, 88.4)
- added REF**: VIA_0.3mm, hp-bldc-pcb:VIA_0.3mm, F.Cu at (114.5, 116.9)
- added REF**: VIA_0.3mm, hp-bldc-pcb:VIA_0.3mm, F.Cu at (154.4, 87.4)
- added REF**: VIA_0.3mm, hp-bldc-pcb:VIA_0.3mm, F.Cu at (154.4, 86.4)
- added REF**: VIA_0.3mm, hp-bldc-pcb:VIA_0.3mm, F.Cu at (154.4, 85.4)
- added REF**: VIA_0.3mm, hp-bldc-pcb:VIA_0.3mm, F.Cu at (154.4, 84.5)
- added REF**: VIA_0.3mm, hp-bldc-pcb:VIA_0.3mm, F.Cu at (154.4, 83.5)
- added REF**: VIA_0.3mm, hp-bldc-pcb:VIA_0.3mm, F.Cu at (154.4, 82.5)
- added REF**: VIA_0.3mm, hp-bldc-pcb:VIA_0.3mm, F.Cu at (153.4, 90.3)
- added REF**: VIA_0.3mm, hp-bldc-pcb:VIA_0.3mm, F.Cu at (153.4, 89.4)
- added REF**: VIA_0.3mm, hp-bldc-pcb:VIA_0.3mm, F.Cu at (153.4, 88.4)
- added REF**: VIA_0.3mm, hp-bldc-pcb:VIA_0.3mm, F.Cu at (153.4, 87.4)
- added REF**: VIA_0.3mm, hp-bldc-pcb:VIA_0.3mm, F.Cu at (108.7, 119.5)
- added REF**: VIA_0.3mm, hp-bldc-pcb:VIA_0.3mm, F.Cu at (153.4, 86.4)
- added REF**: VIA_0.3mm, hp-bldc-pcb:VIA_0.3mm, F.Cu at (153.4, 85.4)
- added REF**: VIA_0.3mm, hp-bldc-pcb:VIA_0.3mm, F.Cu at (153.4, 84.5)
- added REF**: VIA_0.3mm, hp-bldc-pcb:VIA_0.3mm, F.Cu at (153.4, 83.5)
- added REF**: VIA_0.3mm, hp-bldc-pcb:VIA_0.3mm, F.Cu at (153.4, 82.5)
- added REF**: VIA_0.3mm, hp-bldc-pcb:VIA_0.3mm, F.Cu at (152.4, 90.3)
- added REF**: VIA_0.3mm, hp-bldc-pcb:VIA_0.3mm, F.Cu at (152.4, 89.4)
- added REF**: VIA_0.3mm, hp-bldc-pcb:VIA_0.3mm, F.Cu at (152.4, 88.4)
- added REF**: VIA_0.3mm, hp-bldc-pcb:VIA_0.3mm, F.Cu at (152.4, 87.4)
- added REF**: VIA_0.3mm, hp-bldc-pcb:VIA_0.3mm, F.Cu at (152.4, 86.4)
- added REF**: VIA_0.3mm, hp-bldc-pcb:VIA_0.3mm, F.Cu at (156.7, 99.6)
- added REF**: VIA_0.3mm, hp-bldc-pcb:VIA_0.3mm, F.Cu at (152.4, 85.4)
- added REF**: VIA_0.3mm, hp-bldc-pcb:VIA_0.3mm, F.Cu at (152.4, 84.5)
- added REF**: VIA_0.3mm, hp-bldc-pcb:VIA_0.3mm, F.Cu at (152.4, 83.5)
- added REF**: VIA_0.3mm, hp-bldc-pcb:VIA_0.3mm, F.Cu at (152.4, 82.5)
- added REF**: VIA_0.3mm, hp-bldc-pcb:VIA_0.3mm, F.Cu at (151.5, 90.3)
- added REF**: VIA_0.3mm, hp-bldc-pcb:VIA_0.3mm, F.Cu at (151.5, 89.4)
- added REF**: VIA_0.3mm, hp-bldc-pcb:VIA_0.3mm, F.Cu at (151.5, 88.4)
- added REF**: VIA_0.3mm, hp-bldc-pcb:VIA_0.3mm, F.Cu at (151.5, 87.4)
- added REF**: VIA_0.3mm, hp-bldc-pcb:VIA_0.3mm, F.Cu at (151.5, 86.4)
- added REF**: VIA_0.3mm, hp-bldc-pcb:VIA_0.3mm, F.Cu at (151.5, 85.4)
- added REF**: VIA_0.3mm, hp-bldc-pcb:VIA_0.3mm, F.Cu at (139.8, 99.6)
- added REF**: VIA_0.3mm, hp-bldc-pcb:VIA_0.3mm, F.Cu at (151.5, 84.5)
- added REF**: VIA_0.3mm, hp-bldc-pcb:VIA_0.3mm, F.Cu at (151.5, 83.5)
- added REF**: VIA_0.3mm, hp-bldc-pcb:VIA_0.3mm, F.Cu at (151.5, 82.5)
- added REF**: VIA_0.3mm, hp-bldc-pcb:VIA_0.3mm, F.Cu at (150.5, 90.3)
- added REF**: VIA_0.3mm, hp-bldc-pcb:VIA_0.3mm, F.Cu at (150.5, 89.4)
- added REF**: VIA_0.3mm, hp-bldc-pcb:VIA_0.3mm, F.Cu at (150.5, 88.4)
- added REF**: VIA_0.3mm, hp-bldc-pcb:VIA_0.3mm, F.Cu at (150.5, 87.4)
- added REF**: VIA_0.3mm, hp-bldc-pcb:VIA_0.3mm, F.Cu at (150.5, 86.4)
- added REF**: VIA_0.3mm, hp-bldc-pcb:VIA_0.3mm, F.Cu at (150.5, 85.4)
- added REF**: VIA_0.3mm, hp-bldc-pcb:VIA_0.3mm, F.Cu at (150.5, 84.5)
- added REF**: VIA_0.3mm, hp-bldc-pcb:VIA_0.3mm, F.Cu at (122.7, 99.8)
- added REF**: VIA_0.3mm, hp-bldc-pcb:VIA_0.3mm, F.Cu at (150.5, 83.5)
- added REF**: VIA_0.3mm, hp-bldc-pcb:VIA_0.3mm, F.Cu at (150.5, 82.5)
- added REF**: VIA_0.3mm, hp-bldc-pcb:VIA_0.3mm, F.Cu at (149.5, 90.3)
- added REF**: VIA_0.3mm, hp-bldc-pcb:VIA_0.3mm, F.Cu at (149.5, 89.4)
- added REF**: VIA_0.3mm, hp-bldc-pcb:VIA_0.3mm, F.Cu at (149.5, 88.4)
- added REF**: VIA_0.3mm, hp-bldc-pcb:VIA_0.3mm, F.Cu at (149.5, 87.4)
- added REF**: VIA_0.3mm, hp-bldc-pcb:VIA_0.3mm, F.Cu at (149.5, 86.4)
- added REF**: VIA_0.3mm, hp-bldc-pcb:VIA_0.3mm, F.Cu at (149.5, 85.4)
- added REF**: VIA_0.3mm, hp-bldc-pcb:VIA_0.3mm, F.Cu at (149.5, 84.5)
- added REF**: VIA_0.3mm, hp-bldc-pcb:VIA_0.3mm, F.Cu at (149.5, 83.5)
- added REF**: VIA_0.3mm, hp-bldc-pcb:VIA_0.3mm, F.Cu at (98.8, 102.5)
- added REF**: VIA_0.3mm, hp-bldc-pcb:VIA_0.3mm, F.Cu at (98.8, 104.5)
- added REF**: VIA_0.3mm, hp-bldc-pcb:VIA_0.3mm, F.Cu at (98.8, 106.5)
- added REF**: VIA_0.3mm, hp-bldc-pcb:VIA_0.3mm, F.Cu at (183.4, 99.1)
- added REF**: VIA_0.3mm, hp-bldc-pcb:VIA_0.3mm, F.Cu at (98.8, 108.5)
- added REF**: VIA_0.3mm, hp-bldc-pcb:VIA_0.3mm, F.Cu at (98.8, 91.2)
- added REF**: VIA_0.3mm, hp-bldc-pcb:VIA_0.3mm, F.Cu at (98.8, 89.4)
- added REF**: VIA_0.3mm, hp-bldc-pcb:VIA_0.3mm, F.Cu at (98.8, 87.6)
- added REF**: VIA_0.3mm, hp-bldc-pcb:VIA_0.3mm, F.Cu at (98.8, 85.8)
- added REF**: VIA_0.3mm, hp-bldc-pcb:VIA_0.3mm, F.Cu at (104.9, 84.7)
- added REF**: VIA_0.3mm, hp-bldc-pcb:VIA_0.3mm, F.Cu at (107.2, 93.1)
- added REF**: VIA_0.3mm, hp-bldc-pcb:VIA_0.3mm, F.Cu at (107.2, 86.1)
- added REF**: VIA_0.3mm, hp-bldc-pcb:VIA_0.3mm, F.Cu at (107.2, 87.1)
- added REF**: VIA_0.3mm, hp-bldc-pcb:VIA_0.3mm, F.Cu at (107.2, 88.1)
- added REF**: VIA_0.3mm, hp-bldc-pcb:VIA_0.3mm, F.Cu at (181.5, 104.3)
- added REF**: VIA_0.3mm, hp-bldc-pcb:VIA_0.3mm, F.Cu at (161.8, 107.6)
- added REF**: VIA_0.3mm, hp-bldc-pcb:VIA_0.3mm, F.Cu at (161.8, 106.6)
- added REF**: VIA_0.3mm, hp-bldc-pcb:VIA_0.3mm, F.Cu at (161.8, 105.6)
- added REF**: VIA_0.3mm, hp-bldc-pcb:VIA_0.3mm, F.Cu at (161.8, 104.6)
- added REF**: VIA_0.3mm, hp-bldc-pcb:VIA_0.3mm, F.Cu at (161.8, 103.6)
- added REF**: VIA_0.3mm, hp-bldc-pcb:VIA_0.3mm, F.Cu at (149.8, 118.6)
- added REF**: VIA_0.3mm, hp-bldc-pcb:VIA_0.3mm, F.Cu at (148.8, 118.6)
- added REF**: VIA_0.3mm, hp-bldc-pcb:VIA_0.3mm, F.Cu at (147.8, 118.6)
- added REF**: VIA_0.3mm, hp-bldc-pcb:VIA_0.3mm, F.Cu at (146.8, 118.6)
- added REF**: VIA_0.3mm, hp-bldc-pcb:VIA_0.3mm, F.Cu at (149.8, 117.0)
- added REF**: VIA_0.3mm, hp-bldc-pcb:VIA_0.3mm, F.Cu at (158.1, 118.1)
- added REF**: VIA_0.3mm, hp-bldc-pcb:VIA_0.3mm, F.Cu at (148.8, 117.0)
- added REF**: VIA_0.3mm, hp-bldc-pcb:VIA_0.3mm, F.Cu at (147.8, 117.0)
- added REF**: VIA_0.3mm, hp-bldc-pcb:VIA_0.3mm, F.Cu at (146.8, 117.0)
- added REF**: VIA_0.3mm, hp-bldc-pcb:VIA_0.3mm, F.Cu at (149.8, 116.0)
- added REF**: VIA_0.3mm, hp-bldc-pcb:VIA_0.3mm, F.Cu at (148.8, 116.0)
- added REF**: VIA_0.3mm, hp-bldc-pcb:VIA_0.3mm, F.Cu at (147.8, 116.0)
- added REF**: VIA_0.3mm, hp-bldc-pcb:VIA_0.3mm, F.Cu at (139.0, 118.6)
- added REF**: VIA_0.3mm, hp-bldc-pcb:VIA_0.3mm, F.Cu at (138.0, 118.6)
- added REF**: VIA_0.3mm, hp-bldc-pcb:VIA_0.3mm, F.Cu at (137.0, 118.6)
- added REF**: VIA_0.3mm, hp-bldc-pcb:VIA_0.3mm, F.Cu at (146.8, 116.0)
- added REF**: VIA_0.3mm, hp-bldc-pcb:VIA_0.3mm, F.Cu at (128.7, 115.9)
- added REF**: VIA_0.3mm, hp-bldc-pcb:VIA_0.3mm, F.Cu at (139.0, 116.0)
- added REF**: VIA_0.3mm, hp-bldc-pcb:VIA_0.3mm, F.Cu at (138.0, 117.0)
- added REF**: VIA_0.3mm, hp-bldc-pcb:VIA_0.3mm, F.Cu at (138.0, 116.0)
- added REF**: VIA_0.3mm, hp-bldc-pcb:VIA_0.3mm, F.Cu at (139.0, 117.0)
- added REF**: VIA_0.3mm, hp-bldc-pcb:VIA_0.3mm, F.Cu at (137.0, 117.0)
- added REF**: VIA_0.3mm, hp-bldc-pcb:VIA_0.3mm, F.Cu at (137.0, 116.0)
- added REF**: VIA_0.3mm, hp-bldc-pcb:VIA_0.3mm, F.Cu at (136.0, 118.6)
- added REF**: VIA_0.3mm, hp-bldc-pcb:VIA_0.3mm, F.Cu at (136.0, 117.0)
- added REF**: VIA_0.3mm, hp-bldc-pcb:VIA_0.3mm, F.Cu at (136.0, 116.0)
- added REF**: VIA_0.3mm, hp-bldc-pcb:VIA_0.3mm, F.Cu at (160.1, 107.6)
- added REF**: VIA_0.3mm, hp-bldc-pcb:VIA_0.3mm, F.Cu at (161.0, 112.2)
- added REF**: VIA_0.3mm, hp-bldc-pcb:VIA_0.3mm, F.Cu at (160.1, 106.6)
- added REF**: VIA_0.3mm, hp-bldc-pcb:VIA_0.3mm, F.Cu at (160.1, 105.6)
- added REF**: VIA_0.3mm, hp-bldc-pcb:VIA_0.3mm, F.Cu at (160.1, 104.6)
- added REF**: VIA_0.3mm, hp-bldc-pcb:VIA_0.3mm, F.Cu at (160.1, 103.6)
- added REF**: VIA_0.3mm, hp-bldc-pcb:VIA_0.3mm, F.Cu at (154.0, 107.6)
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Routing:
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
